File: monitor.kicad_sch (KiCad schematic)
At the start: 54 parts, among them J71 Conn_01x01_Socket, J72 Conn_01x01_Socket, J73 Conn_01x01_Socket, J74 Conn_01x01_Socket, J75 Conn_01x01_Socket, J76 Conn_01x01_Socket, U704 OPA2197D, U71 TMUX6104, U72 TMUX6104, U76 OPA2189DGK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

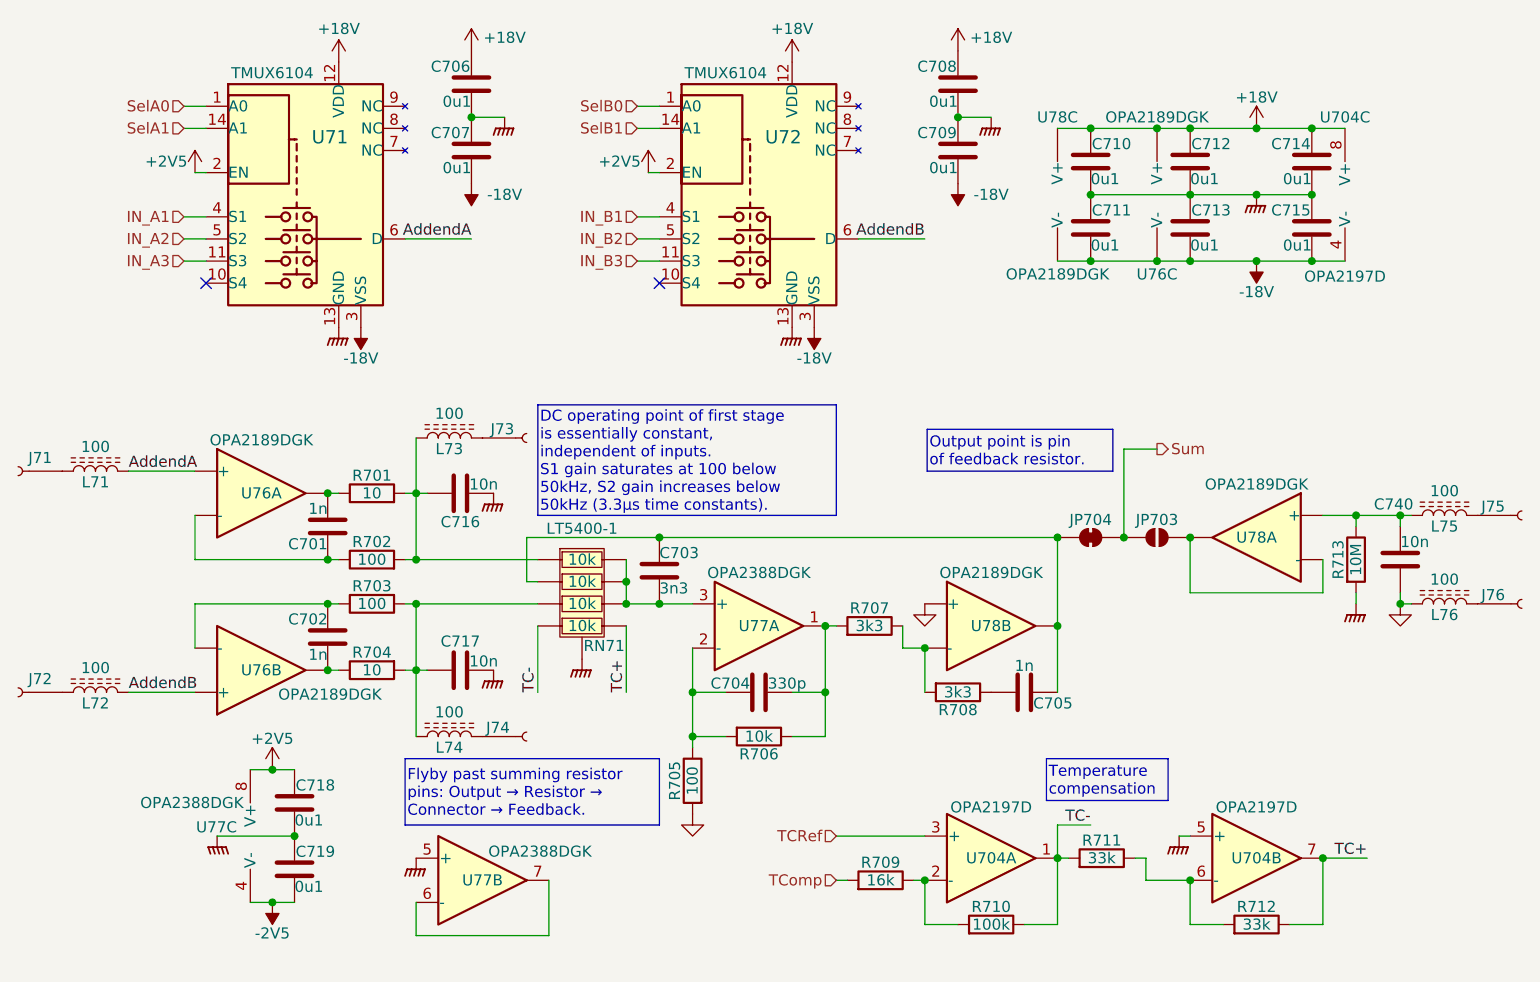
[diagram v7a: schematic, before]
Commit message: Tweaks following spice simulation.
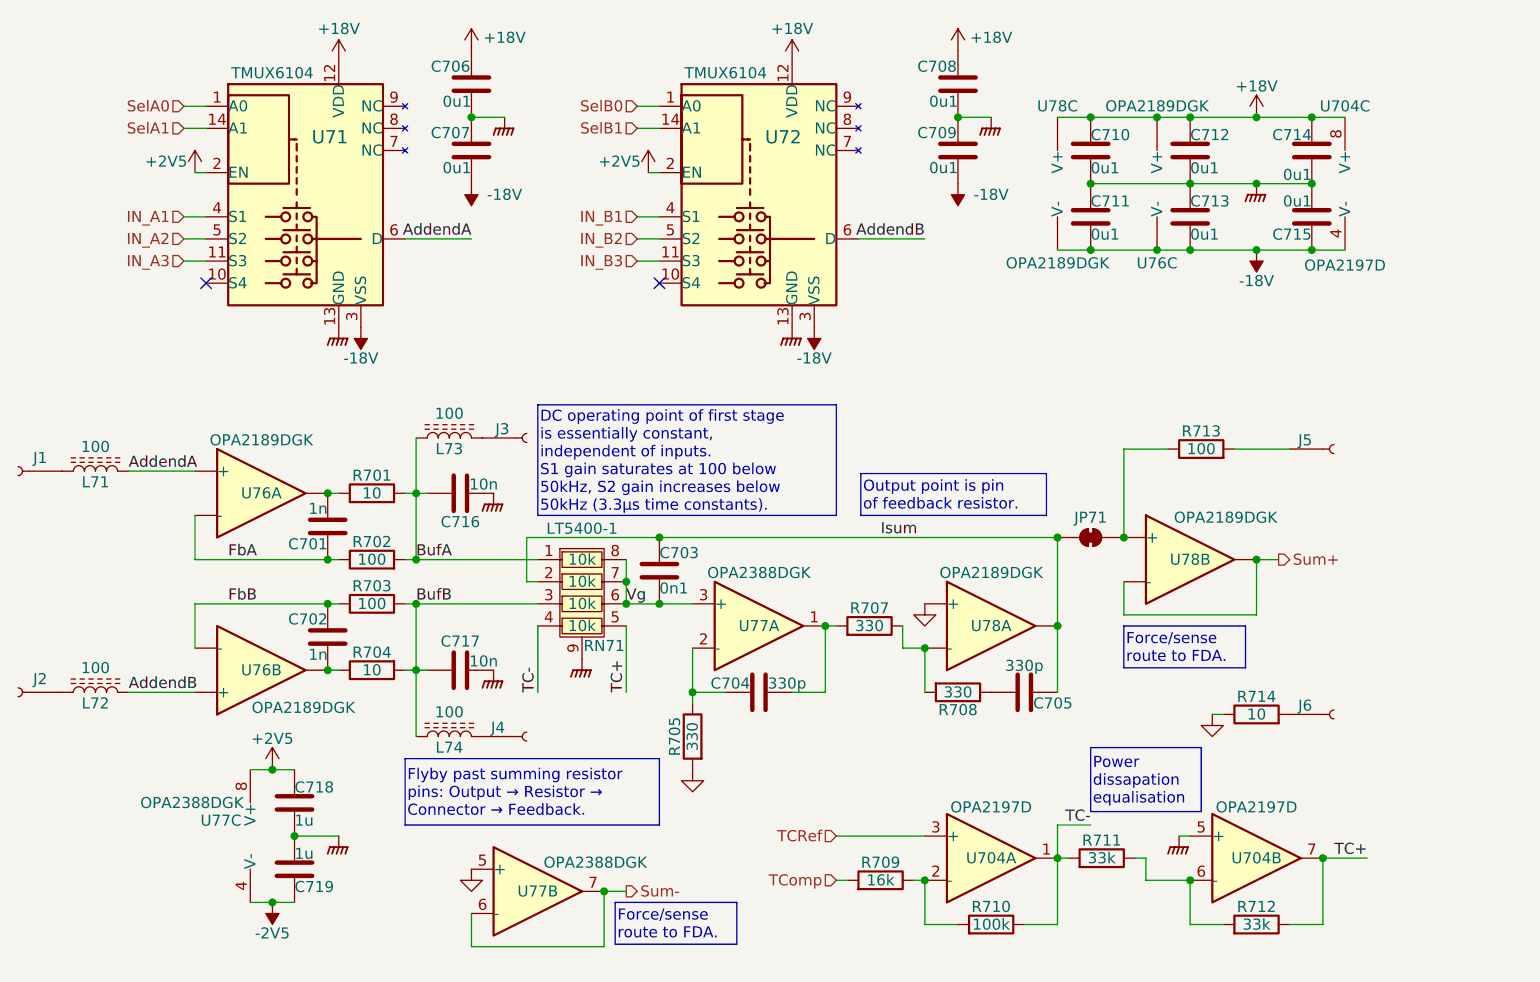
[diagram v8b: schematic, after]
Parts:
- removed C740: 10n, Capacitor_SMD:C_0603_1608Metric, symbol Device:C
- removed JP703: SolderJumper_2_Open, Parts:ThermJump_1, symbol Jumper:SolderJumper_2_Open
- removed JP704: SolderJumper_2_Bridged, Parts:ThermJumpBridge, symbol Jumper:SolderJumper_2_Bridged
- removed L75, L76: 100, Inductor_SMD:L_0603_1608Metric, symbol Device:L_Ferrite
- removed R706: 10k, Resistor_SMD:R_0603_1608Metric, symbol Device:R
- added JP71: SolderJumper_2_Bridged, Parts:JumperClosed, symbol Jumper:SolderJumper_2_Bridged
- added R714: 10, Resistor_SMD:R_0402_1005Metric, symbol Device:R
- C703: value 3n3 -> 0n1; LCSC (none) -> C1546; now in the parts list
- C705: value 1n -> 330p; LCSC (none) -> C1664
- C718, C719: value 0u1 -> 1u; LCSC C307331 -> C52923
- J1: renamed from J71; footprint TestPoint:TestPoint_Plated_Hole_D5.0mm -> Parts:Plated_Hole_D4.0mm_10mm
- J2: renamed from J72; footprint TestPoint:TestPoint_Plated_Hole_D5.0mm -> Parts:Plated_Hole_D4.0mm_10mm
- J3: renamed from J73; footprint TestPoint:TestPoint_Plated_Hole_D5.0mm -> Parts:Plated_Hole_D4.0mm_10mm
- J4: renamed from J74; footprint TestPoint:TestPoint_Plated_Hole_D5.0mm -> Parts:Plated_Hole_D4.0mm_10mm
- J5: renamed from J75; footprint TestPoint:TestPoint_Plated_Hole_D5.0mm -> Parts:Plated_Hole_D4.0mm_10mm
- J6: renamed from J76; footprint TestPoint:TestPoint_Plated_Hole_D5.0mm -> Parts:Plated_Hole_D4.0mm_10mm
- R705: value 100 -> 330; footprint Resistor_SMD:R_0603_1608Metric -> Resistor_SMD:R_0402_1005Metric; LCSC C23140 -> C25104
- R707, R708: value 3k3 -> 330; footprint Resistor_SMD:R_0603_1608Metric -> Resistor_SMD:R_0402_1005Metric; LCSC C22978 -> C25104
- R713: value 10M -> 100; footprint Resistor_SMD:R_0603_1608Metric -> Resistor_SMD:R_0402_1005Metric; LCSC C7250 -> C25076
- RN71: footprint Package_SO:MSOP-8-1EP_3x3mm_P0.65mm_EP1.68x1.88mm -> Parts:MSOP-8-1EP_3x3mm_P0.65mm_EP1.68x1.88mm
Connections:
- net GND: now also U77.5 (+), U78.3 (+), R714.1; no longer U78.5 (+)
- net GNDPWR: no longer R713.2, U77.5 (+)
- net at R713.1: now also U78.5 (+), JP71.2 (B); no longer U78.3 (+)
- net BufB: now reaches C717.2, L74.1, R703.2, R704.2, RN71.3
- net FbB: now reaches C702.1, R703.1, U76.6 (-)
- net FbA: now reaches C701.2, R702.1, U76.2 (-)
- net Isum: now reaches C703.1, C705.2, RN71.2
- net Isum: now also U78.1, JP71.1 (A); no longer U78.7
- net BufA: now reaches C716.2, L73.1, R701.2, R702.2, RN71.1
- net Vg: now reaches C703.2, RN71.6, RN71.7, RN71.8, U77.3 (+)
- net at J6.1 (Pin_1): now also R714.2
- net at R707.1, R708.2: now also U78.2 (-); no longer U78.6 (-)
- net at J5.1 (Pin_1): now also R713.2
- net Sum-: now reaches U77.6 (-), U77.7
- new net Sum+: U78.6 (-), U78.7
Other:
- moved on the sheet: C710, C711, C712, C713, C714, C715, J5, J6, R705, U704C, U76C, U77B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
